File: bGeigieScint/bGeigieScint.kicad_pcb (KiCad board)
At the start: 4 copper layers, 40 x 100 mm, 174 parts, among them P1 Header-Male-2.54_2x2, P2 Header-Male-2.54_2x2, Q1 BC847_C2910145, Q2 MMBT5551LT1G, Q3 AO3401A, Q4 AO3401A, Q5 MMBT5551LT1G, U1 ATSAML21G18B-AUT, U10 74LVC1G08GV,125, U11 LT3014BHVES5#TRMPBF, U12 TXU0202DCUR, U13 TLV7031DBVR, U14 TLR341G-GTR, U15 803-87-006-10-001101, U2 XC6209F332MR-G, U3 MC14043BDR2G, U4 LMV793MFX/NOPB, U5 TPS7A2030PDBVR, U6 TLV3201AIDBVT, U7 OPA357AIDBVR, U8 TLR341G-GTR, U9 MF-ASML020/6-2, X1 32.768kHz

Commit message: Add initial project file for bGeigieScint design
- Created bGeigieScint.kicad_prl file to define project settings and configurations.
- Configured board properties including active layer, visibility settings, and opacity.
- Set up net inspector panel preferences for better net management.
- Included schematic selection filters for improved design navigation.
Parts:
- U1: value ATSAML21G18B-AUT -> ESP32-C3-MINI-1
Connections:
- C11 pad 2: 3V0 -> 3V3
- C15 pad 2: SHAPER_OUT -> Net-(U7-IN+)
- C2 pad 2: 3V0 -> 3V3
- C3 pad 2: 3V0 -> 3V3
- H5 pad 3: SHAPER_OUT -> Net-(U4-OUTPUT)
- MEAS1 pad 2: 3V3 -> Net-(MEAS1-Pad2)
- R17 pad 1: SHAPER_OUT -> Net-(U4-OUTPUT)
- R17 pad 2: SHAPER_OUT -> Net-(U7-IN+)
- R19 pad 2: SHAPER_OUT -> Net-(U4-OUTPUT)
- R27 pad 1: Net-(U10-Y) -> 3V3
- TP10 pad 1: SHAPER_OUT -> Net-(U4-OUTPUT)
- TP7 pad 1: 3V3 -> Net-(MEAS1-Pad2)
- U10 pad 4: Net-(U10-Y) -> 3V3
- U4 pad 1: SHAPER_OUT -> Net-(U4-OUTPUT)
- U6 pad 3: SHAPER_OUT -> Net-(U4-OUTPUT)
- U7 pad 3: SHAPER_OUT -> Net-(U7-IN+)

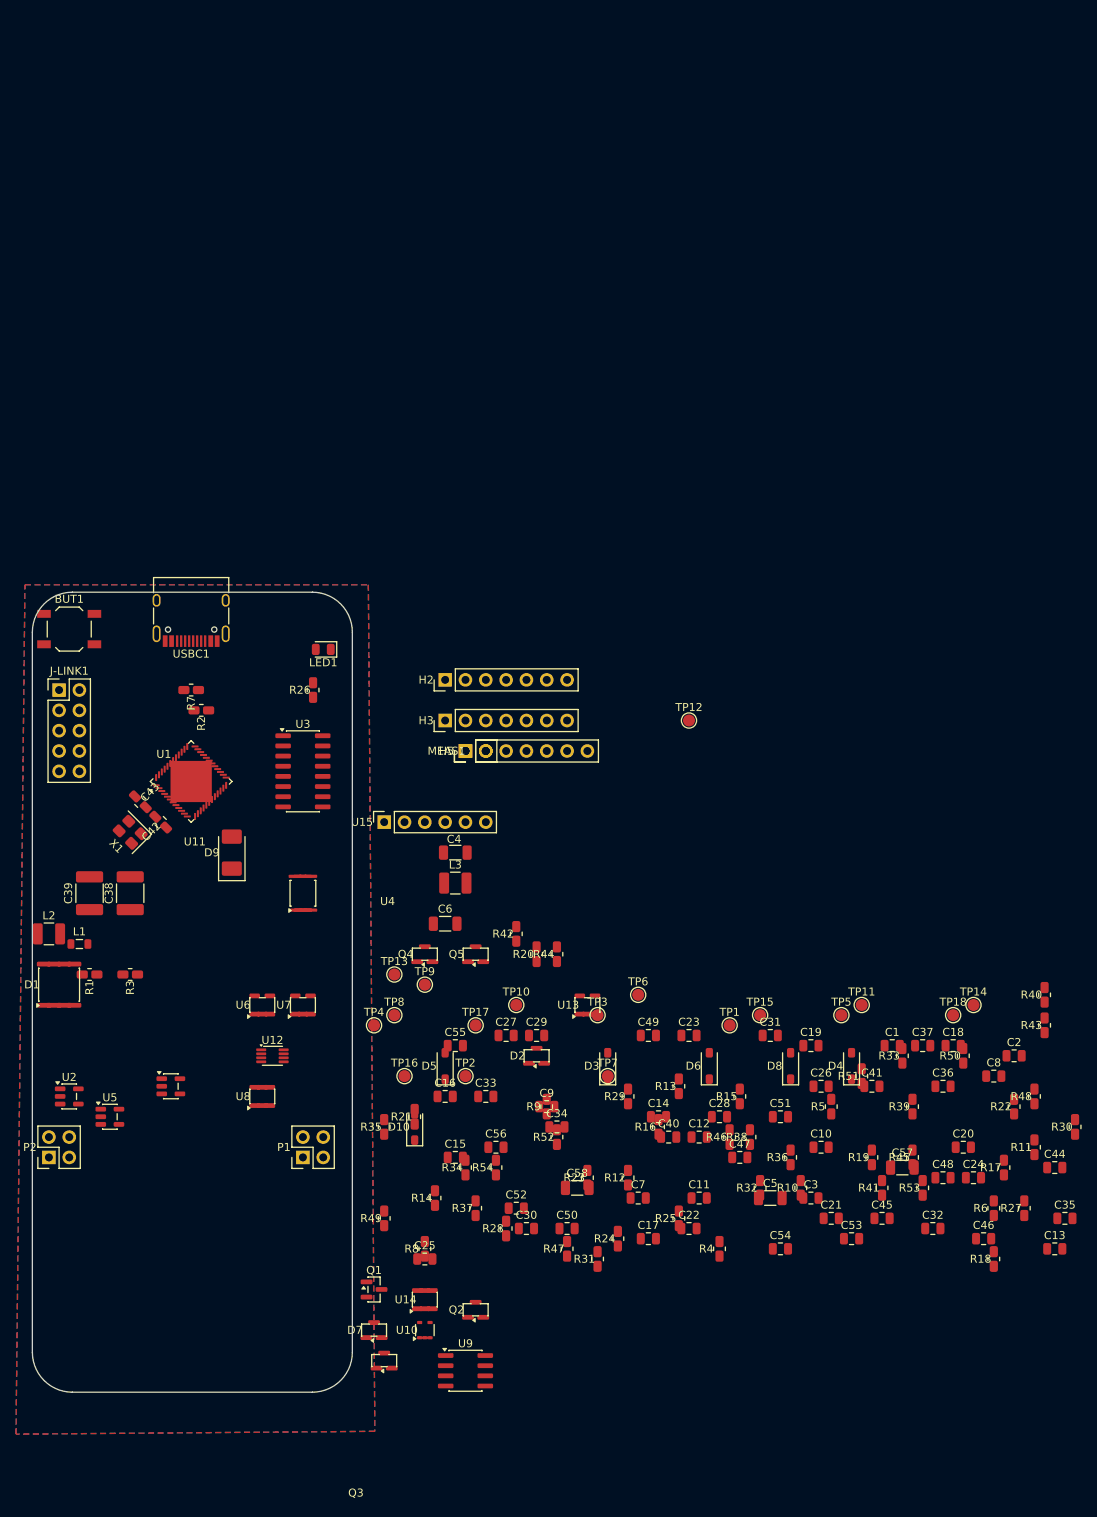
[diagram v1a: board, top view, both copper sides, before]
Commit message: Progress  on switching the ESP32 C3 supper mini
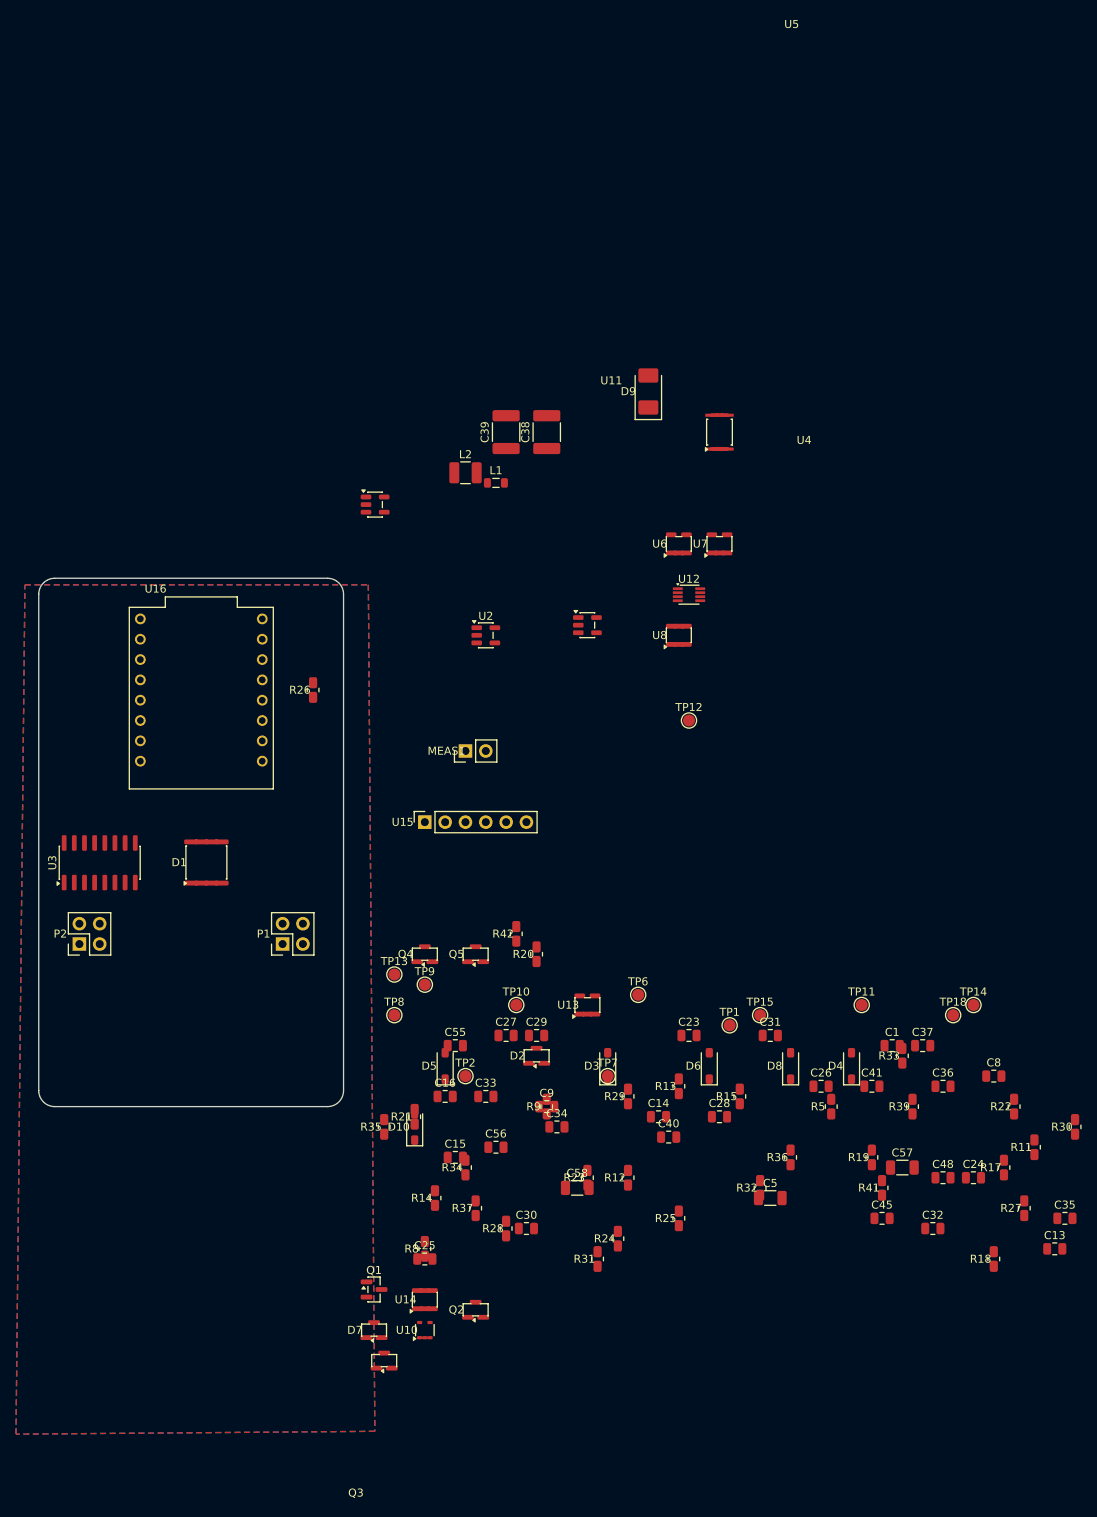
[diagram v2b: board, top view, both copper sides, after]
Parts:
- removed BUT1: TS-1187A-B-A-B, Button_Switch_SMD:SW_SPST_TL3342
- removed C10: 4.7nF, Capacitor_SMD:C_0805_2012Metric
- removed C11, C12, C18, C21, C46, C50, C51, C53, C7: 100nF, Capacitor_SMD:C_0805_2012Metric
- removed C17, C2, C22: 10nF, Capacitor_SMD:C_0805_2012Metric
- removed C19, C20, C3, C44, C47, C49, C52, C54: 4.7uF, Capacitor_SMD:C_0805_2012Metric
- removed C4, C6: 10uF, Capacitor_SMD:C_1206_3216Metric
- removed C42, C43: 18pF, Capacitor_SMD:C_0805_2012Metric
- removed H2, H3, H5: KH-2.54PH180-1X7P-L11.5, Connector_PinHeader_2.54mm:PinHeader_1x07_P2.54mm_Vertical
- removed J-LINK1: 20021111-00010T4LF, Connector_PinHeader_2.54mm:PinHeader_2x05_P2.54mm_Vertical
- removed L3: 470Ω, Inductor_SMD:L_1210_3225Metric
- removed LED1: 19-217/GHC-YR1S2/3T, LED_SMD:LED_0805_2012Metric
- removed R1: 27kΩ, Resistor_SMD:R_0805_2012Metric
- removed R10: 100Ω, Resistor_SMD:R_0805_2012Metric
- removed R16: 100kΩ, Resistor_SMD:R_0805_2012Metric
- removed R2, R7: 5.1kΩ, Resistor_SMD:R_0805_2012Metric
- removed R3: 47kΩ, Resistor_SMD:R_0805_2012Metric
- removed R38: 0Ω, Resistor_SMD:R_0805_2012Metric
- removed R4, R40, R43, R44, R45, R46, R47, R48, R49, R50, R51, R52, R53, R54: 1kΩ, Resistor_SMD:R_0805_2012Metric
- removed R6: 1MΩ, Resistor_SMD:R_0805_2012Metric
- removed TP16, TP17, TP3, TP4, TP5: 1-POINT TEST POINT, TestPoint:TestPoint_Pad_D1.5mm
- removed U1: ESP32-C3-MINI-1, Package_DFN_QFN:QFN-48-1EP_7x7mm_P0.5mm_EP5.15x5.15mm
- removed U9: MF-ASML020/6-2, Package_SO:SOIC-8_3.9x4.9mm_P1.27mm
- removed USBC1: USB3.1C16PFSMT, Connector_USB:USB_C_Receptacle_HRO_TYPE-C-31-M-12
- removed X1: 32.768kHz, Crystal:Crystal_SMD_3225-4Pin_3.2x2.5mm
- added U16: ESP32-C3_SUPERMINI_TH, bGeigieScint:MODULE_ESP32-C3_SUPERMINI_TH, F.Cu at (71.1, 63.2)
- moved U5 83.4 mm to (92.8, 39.0)
- moved U12 77.7 mm to (132.1, 50.3)
- moved U2 77.7 mm to (106.7, 55.4)
- moved U8 77.7 mm to (130.8, 55.4)
- moved C38 77.7 mm to (114.3, 30.0)
- moved C39 77.7 mm to (109.2, 30.0)
- moved L1 77.7 mm to (108.0, 36.3)
- moved L2 77.7 mm to (104.1, 35.1)
- moved U11 77.7 mm to (119.4, 54.1)
- moved U6 77.7 mm to (130.8, 44.0)
- moved D9 77.7 mm to (127.0, 24.9)
- moved U4 77.7 mm to (135.9, 30.0)
- moved U7 77.7 mm to (135.9, 44.0)
- moved U3 27.9 mm to (58.4, 83.8), turned to 90 degrees
- moved P2 26.9 mm to (55.9, 94.0)
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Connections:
- C45 pad 2: Net-(U1-VDDCORE) -> unconnected-(C45-Pad2)
- C48 pad 2: Net-(U1-VDDANA) -> 3V3
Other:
- board size 40 x 100 mm -> 38.1 x 66 mm
